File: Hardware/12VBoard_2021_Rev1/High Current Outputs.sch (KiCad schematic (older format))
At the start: 6 parts

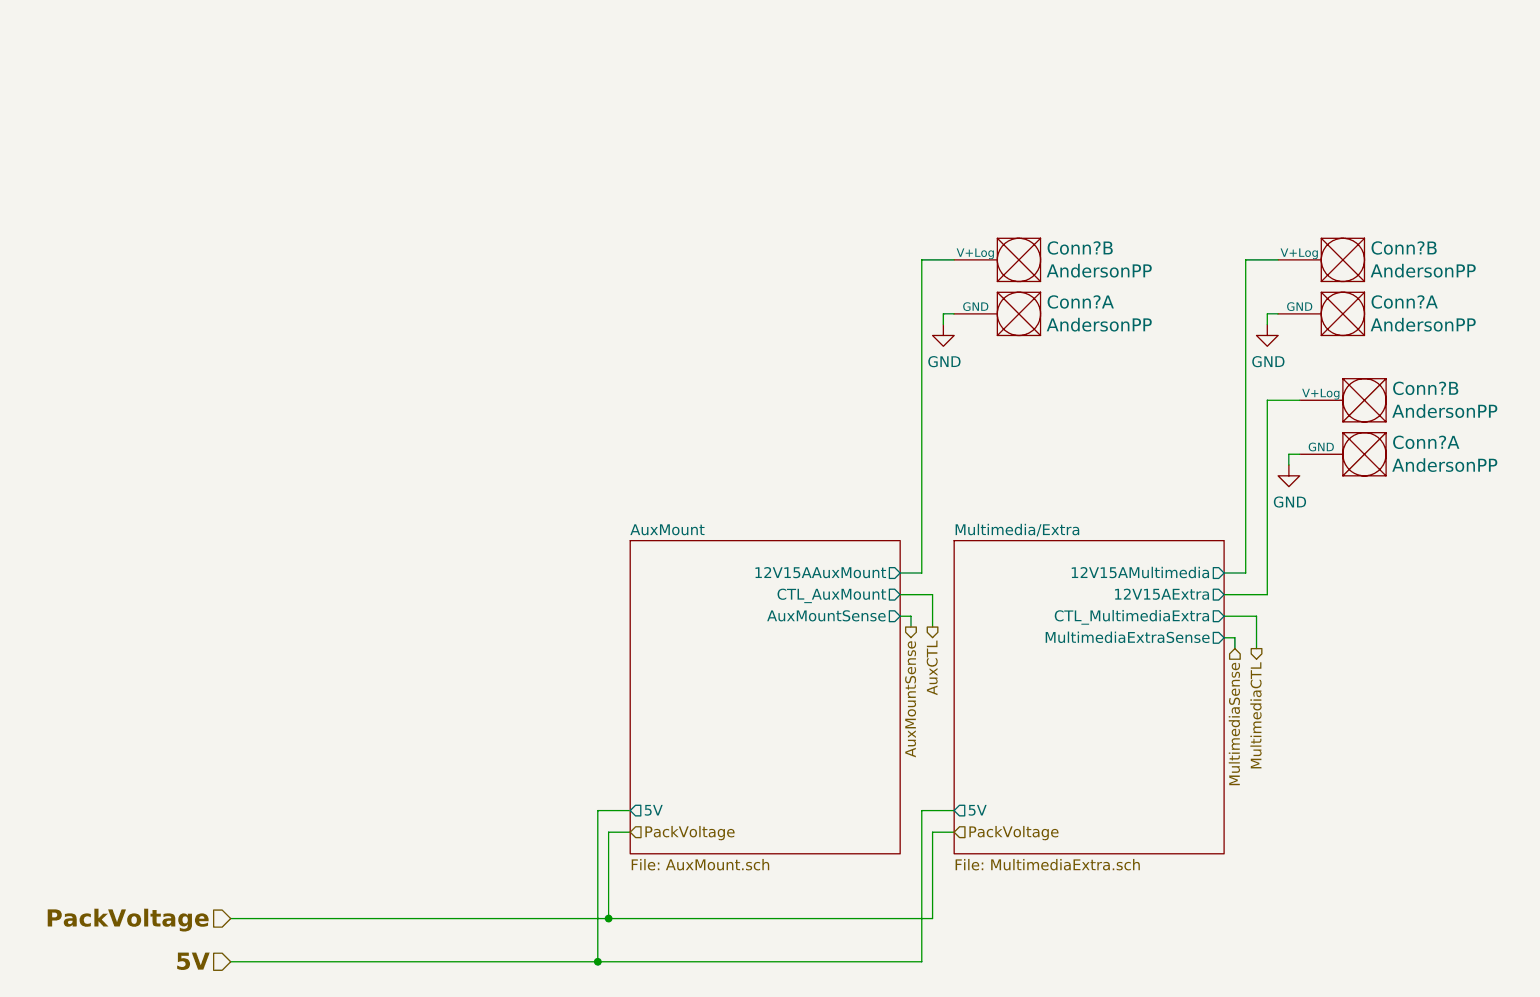
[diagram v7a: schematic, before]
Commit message: fixed High current for second review
addes gimbal to high current. added teva digital write pin to gimbal fot CTL. changed ports from 15 to 10 amp
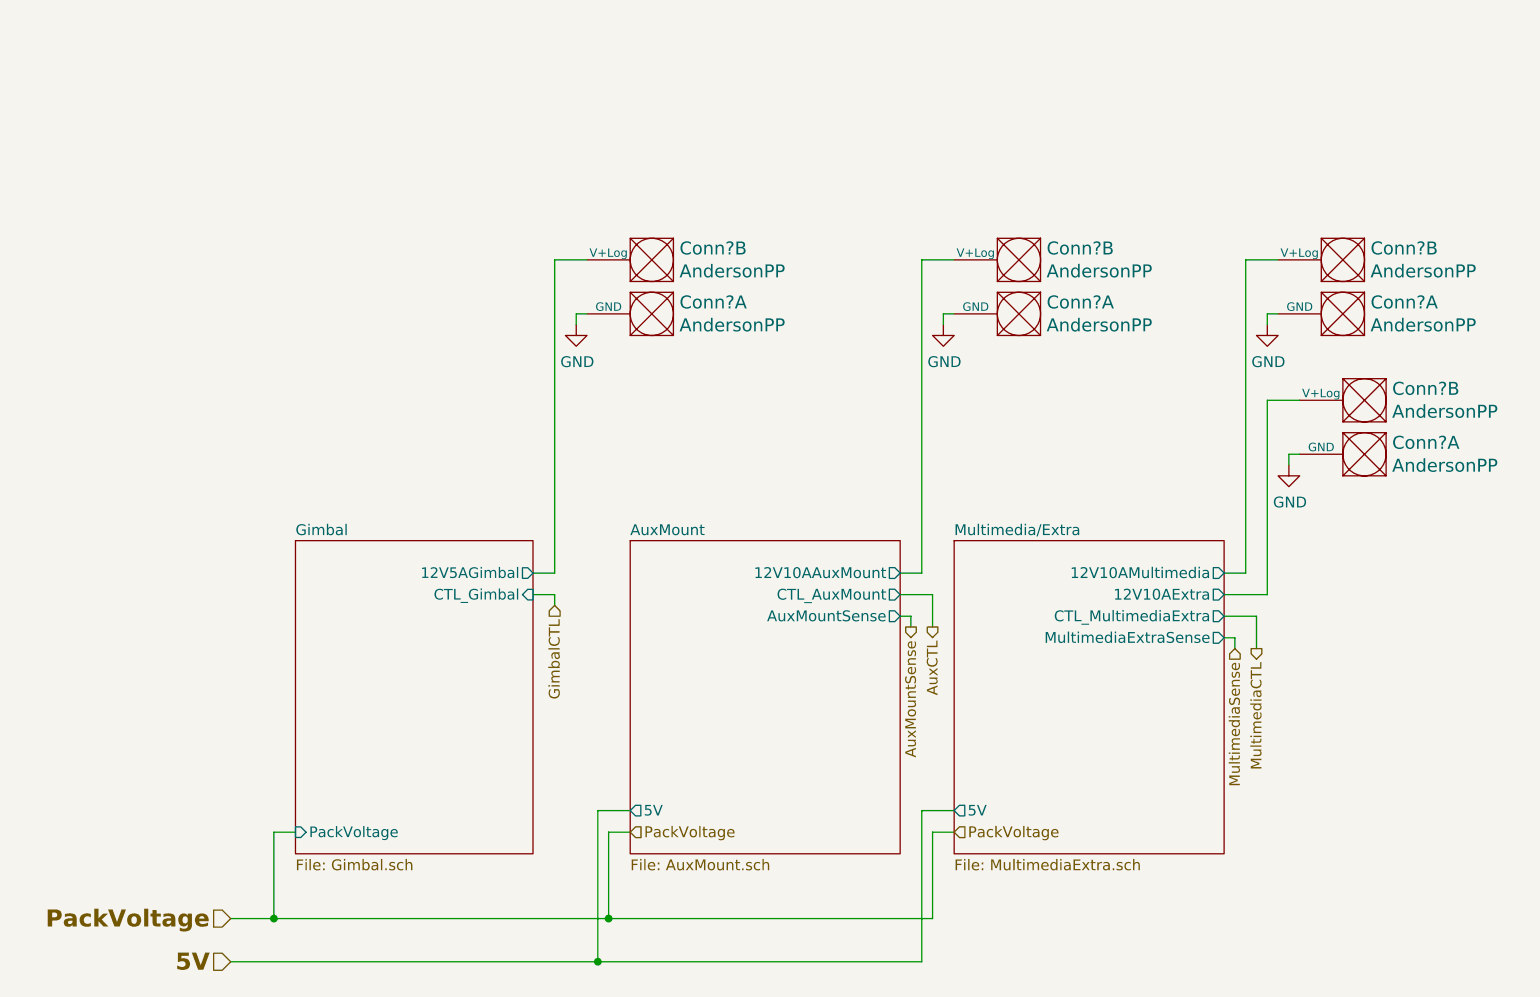
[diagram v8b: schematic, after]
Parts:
- added Conn? (x2): AndersonPP, symbol MRDT_Connectors:AndersonPP
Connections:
- net GND: now also Conn?.1 (GND)
- net AuxMount/12V15AAuxMount renamed AuxMount/12V10AAuxMount
- net Multimedia/Extra/12V15AExtra renamed Multimedia/Extra/12V10AExtra
- net Multimedia/Extra/12V15AMultimedia renamed Multimedia/Extra/12V10AMultimedia
- new net Gimbal/12V5AGimbal: Conn?.2 (V+Log)
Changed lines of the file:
@@
 $Descr A4 11693 8268
 encoding utf-8
-Sheet 5 7
+Sheet 5 8
 Title ""
 Date ""
@@
 F0 "Multimedia/Extra" 50
 F1 "MultimediaExtra.sch" 50
-F2 "12V15AMultimedia" O R 6000 3100 50
+F2 "12V10AMultimedia" O R 6000 3100 50
 F3 "CTL_MultimediaExtra" O R 6000 3300 50
-F4 "12V15AExtra" O R 6000 3200 50
+F4 "12V10AExtra" O R 6000 3200 50
 F5 "MultimediaExtraSense" O R 6000 3400 50
 F6 "5V" O L 4750 4200 49
@@
 F0 "AuxMount" 50
 F1 "AuxMount.sch" 50
-F2 "12V15AAuxMount" O R 4500 3100 50
+F2 "12V10AAuxMount" O R 4500 3100 50
 F3 "CTL_AuxMount" O R 4500 3200 50
 F4 "AuxMountSense" O R 4500 3300 50
@@
 	6150 3300 6150 3450
 Wire Wire Line
-	1400 4700 3150 4700
+	1400 4700 1600 4700
 Wire Wire Line
 	1400 4900 3100 4900
+$Sheet
+S 1700 2950 1100 1450
+U 5F971CD6
+F0 "Gimbal" 50
+F1 "Gimbal.sch" 50
+F2 "CTL_Gimbal" I R 2800 3200 49
+F3 "12V5AGimbal" O R 2800 3100 49
+F4 "PackVoltage" I L 1700 4300 49
+$EndSheet
+Text HLabel 2900 3250 3    50   Input ~ 0
+GimbalCTL
+Wire Wire Line
+	2900 3250 2900 3200
+Wire Wire Line
+	2900 3200 2800 3200
+$Comp
+L MRDT_Connectors:AndersonPP Conn?
+U 1 1 5F978C0F
+P 3450 1800
+AR Path="/5F74F36B/5F821EB2/5F978C0F" Ref="Conn?"  Part="1"
+AR Path="/5F74F36B/5F978C0F" Ref="Conn?"  Part="1"
+F 0 "Conn?" H 3422 1847 60  0000 R CNN
+F 1 "AndersonPP" H 3422 1953 60  0000 R CNN
+F 2 "" H 3300 1250 60  0001 C CNN
+F 3 "" H 3300 1250 60  0001 C CNN
+	1    3450 1800
+	-1   0    0    1
+$EndComp
+$Comp
+L MRDT_Connectors:AndersonPP Conn?
+U 2 1 5F978C15
+P 3450 1550
+AR Path="/5F74F36B/5F821EB2/5F978C15" Ref="Conn?"  Part="2"
+AR Path="/5F74F36B/5F978C15" Ref="Conn?"  Part="2"
+F 0 "Conn?" H 3422 1597 60  0000 R CNN
+F 1 "AndersonPP" H 3422 1703 60  0000 R CNN
+F 2 "" H 3300 1000 60  0001 C CNN
+F 3 "" H 3300 1000 60  0001 C CNN
+	2    3450 1550
+	-1   0    0    1
+$EndComp
+$Comp
+L power:GND #PWR?
+U 1 1 5F978C1B
+P 3000 1950
+AR Path="/5F74F36B/5F821EB2/5F978C1B" Ref="#PWR?"  Part="1"
+AR Path="/5F74F36B/5F978C1B" Ref="#PWR?"  Part="1"
+F 0 "#PWR?" H 3000 1700 50  0001 C CNN
+F 1 "GND" H 3005 1777 50  0000 C CNN
+F 2 "" H 3000 1950 50  0001 C CNN
+F 3 "" H 3000 1950 50  0001 C CNN
+	1    3000 1950
+	1    0    0    -1
+$EndComp
+Wire Wire Line
+	3050 1900 3000 1900
+Wire Wire Line
+	3000 1900 3000 1950
+Wire Wire Line
+	2900 3100 2900 1650
+Wire Wire Line
+	2900 1650 3050 1650
+Wire Wire Line
+	2900 3100 2800 3100
+Wire Wire Line
+	1700 4300 1600 4300
+Wire Wire Line
+	1600 4300 1600 4700
+Connection ~ 1600 4700
+Wire Wire Line
+	1600 4700 3150 4700
 $EndSCHEMATC
